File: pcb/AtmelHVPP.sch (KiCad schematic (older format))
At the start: 20 parts, among them J1 CONN_01X16, J2 CONN_01X16, J3 CONN_01X08, J4 CONN_01X06, J5 CONN_01X10, J6 CONN_01X08, Q1 BC557, Q2 BC547, Q3 BC557, SW1 SW_Push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

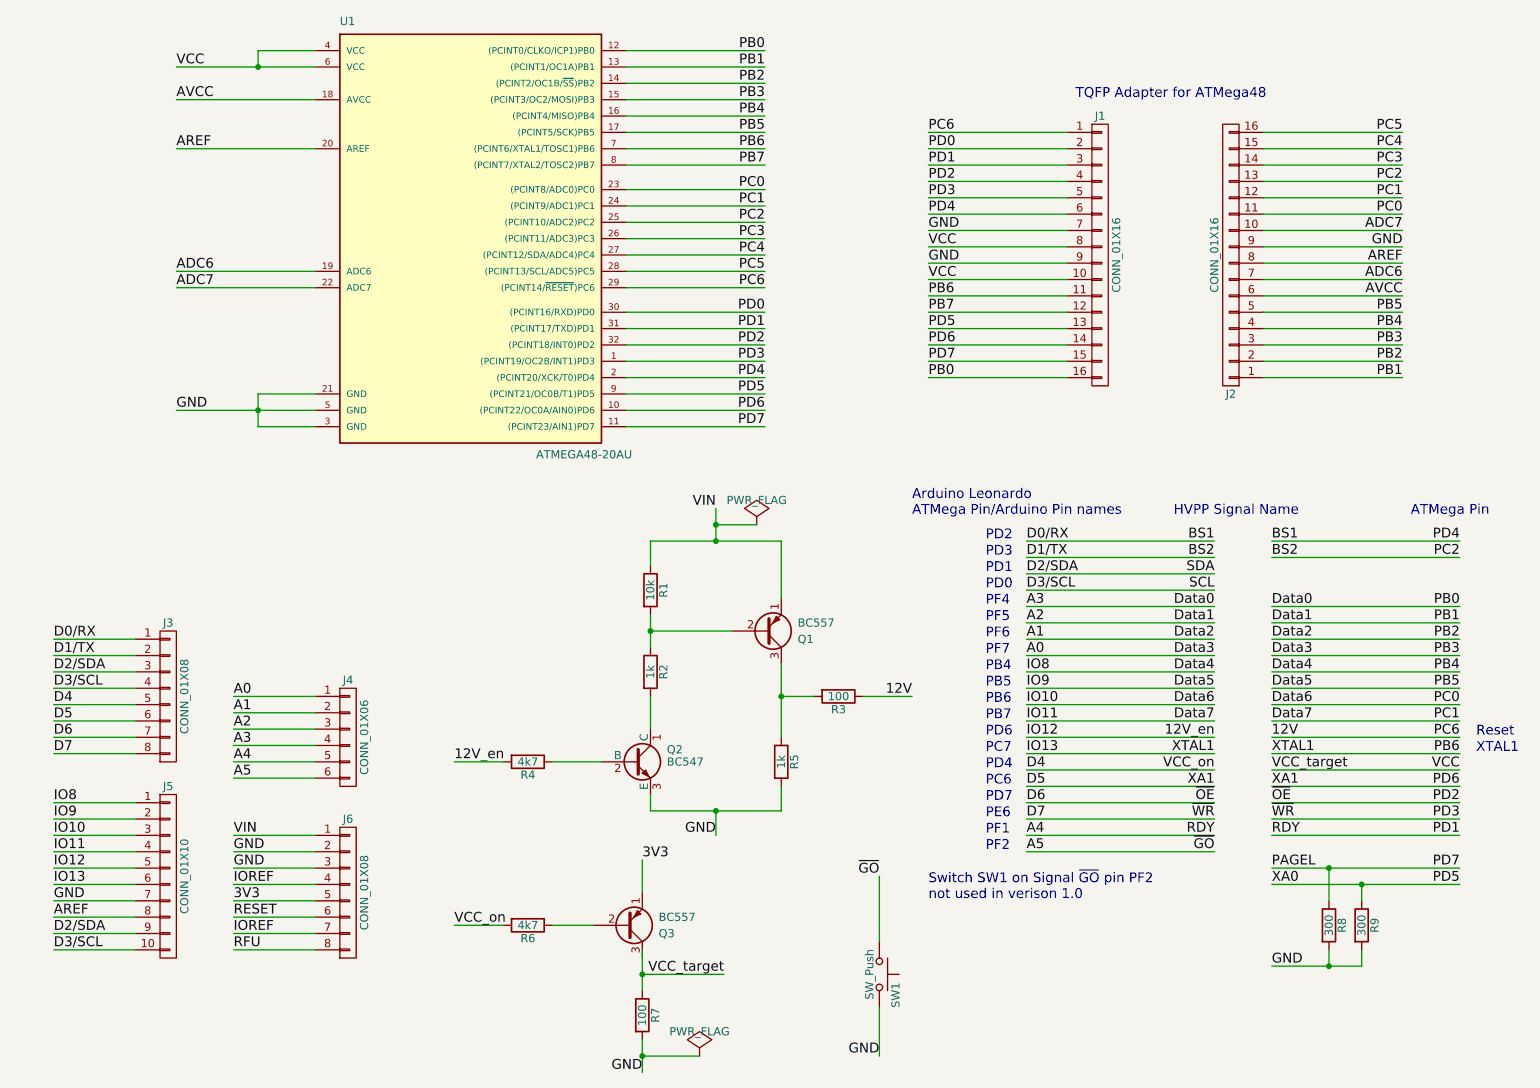
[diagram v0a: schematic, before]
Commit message: Add resistors into connection to Atmel chip with defect fuses for current limitation
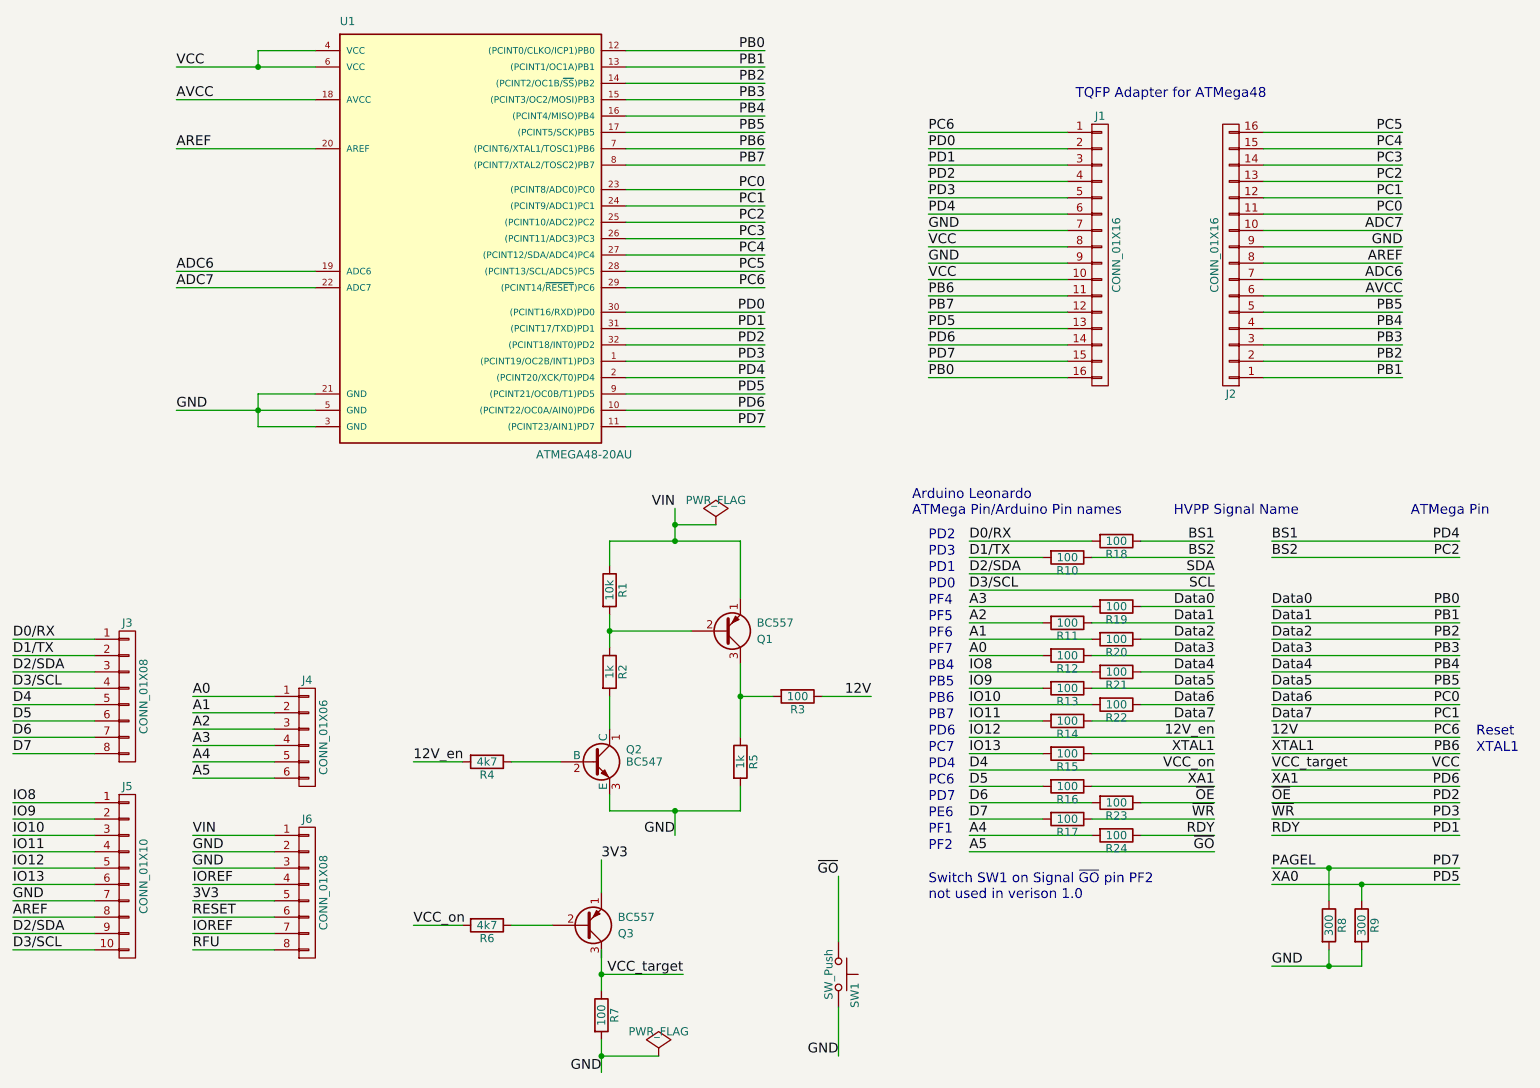
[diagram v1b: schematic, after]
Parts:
- added R10, R11, R12, R13, R14, R15, R16, R17, R18, R19, R20, R21, R22, R23, R24: 100, symbol R
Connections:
- net A0: now also R12.2; no longer J2.3 (P3), U1.15 ((PCINT3/OC2/MOSI)PB3)
- net A1: now also R20.2; no longer J2.2 (P2), U1.14 ((PCINT2/OC1B/~SS~)PB2)
- net A2: now also R11.2; no longer J2.1 (P1), U1.13 ((PCINT1/OC1A)PB1)
- net A3: now also R19.2; no longer J1.16 (P16), U1.12 ((PCINT0/CLKO/ICP1)PB0)
- net A4: now also R24.2; no longer J1.3 (P3), U1.31 ((PCINT17/TXD)PD1)
- net BS1: now also R18.1; no longer J3.1 (P1)
- net BS2: now also R10.1; no longer J3.2 (P2)
- net D5: now also R16.2; no longer J1.14 (P14), U1.10 ((PCINT22/OC0A/AIN0)PD6)
- net D6: now also R23.2; no longer J1.4 (P4), U1.32 ((PCINT18/INT0)PD2)
- net D7: now also R17.2; no longer J1.5 (P5), U1.1 ((PCINT19/OC2B/INT1)PD3)
- net Data4: now also R21.1; no longer J5.1 (P1)
- net Data5: now also R13.1; no longer J5.2 (P2)
- net Data6: now also R22.1; no longer J5.3 (P3)
- net Data7: now also R14.1; no longer J5.4 (P4)
- net IO13: now also R15.2; no longer J1.11 (P11), U1.7 ((PCINT6/XTAL1/TOSC1)PB6)
- new net D0/RX: J3.1 (P1), R18.2
- new net D1/TX: J3.2 (P2), R10.2
- new net Data0: J1.16 (P16), R19.1, U1.12 ((PCINT0/CLKO/ICP1)PB0)
- new net Data1: J2.1 (P1), R11.1, U1.13 ((PCINT1/OC1A)PB1)
- new net Data2: J2.2 (P2), R20.1, U1.14 ((PCINT2/OC1B/~SS~)PB2)
- new net Data3: J2.3 (P3), R12.1, U1.15 ((PCINT3/OC2/MOSI)PB3)
- new net IO10: J5.3 (P3), R22.2
- new net IO11: J5.4 (P4), R14.2
- new net IO8: J5.1 (P1), R21.2
- new net IO9: J5.2 (P2), R13.2
- new net PB6: J1.11 (P11), R15.1, U1.7 ((PCINT6/XTAL1/TOSC1)PB6)
- new net PD1: J1.3 (P3), R24.1, U1.31 ((PCINT17/TXD)PD1)
- new net PD2: J1.4 (P4), R23.1, U1.32 ((PCINT18/INT0)PD2)
- new net PD3: J1.5 (P5), R17.1, U1.1 ((PCINT19/OC2B/INT1)PD3)
- new net PD6: J1.14 (P14), R16.1, U1.10 ((PCINT22/OC0A/AIN0)PD6)
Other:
- moved on the sheet: J3, J4, J5, J6, Q1, Q2, Q3, R1, R2, R3, R4, R5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
